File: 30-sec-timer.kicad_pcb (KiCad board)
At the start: 2 copper layers, 53.3 x 52.1 mm, 30 parts, among them P1 6.3V AC IN, P2 CL12345, P3 Right, P4 Left, Q1 BC557, Q2 BC547, U1 LM7805CT, U2 LM555N

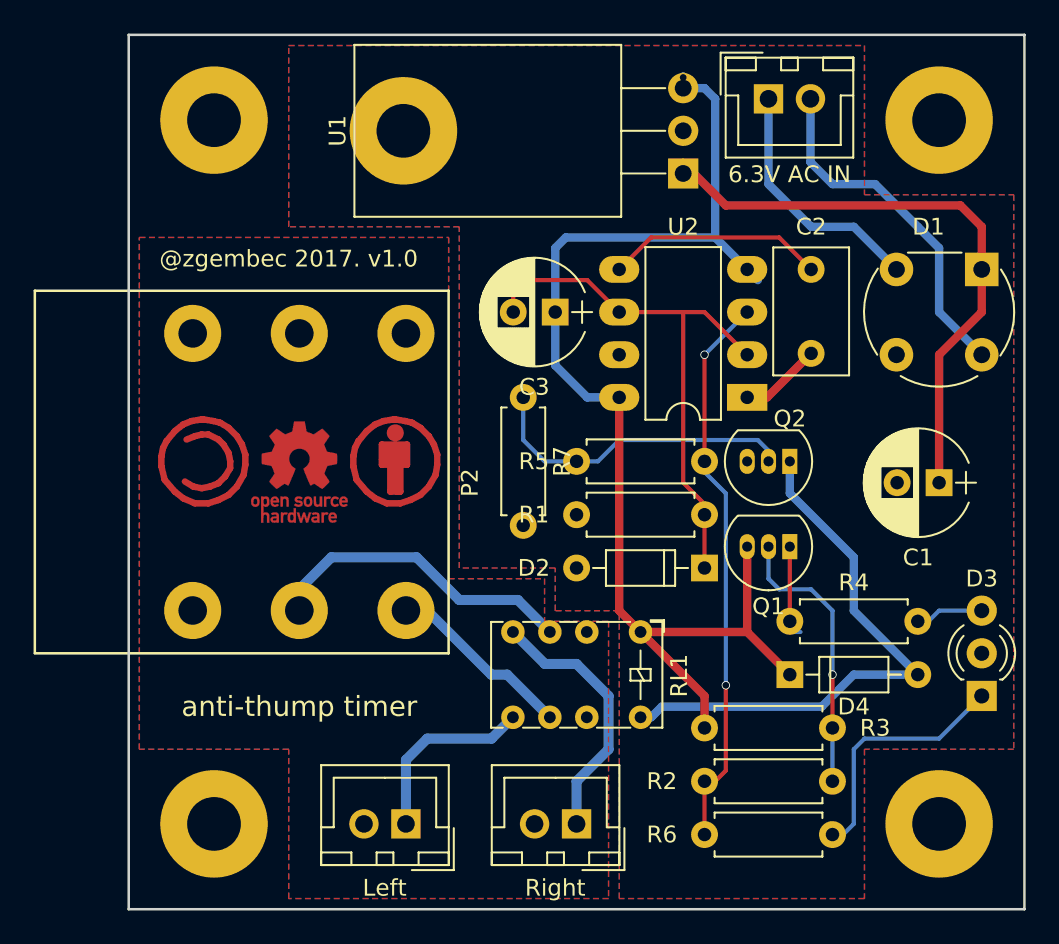
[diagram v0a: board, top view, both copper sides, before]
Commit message: resistor placement fix
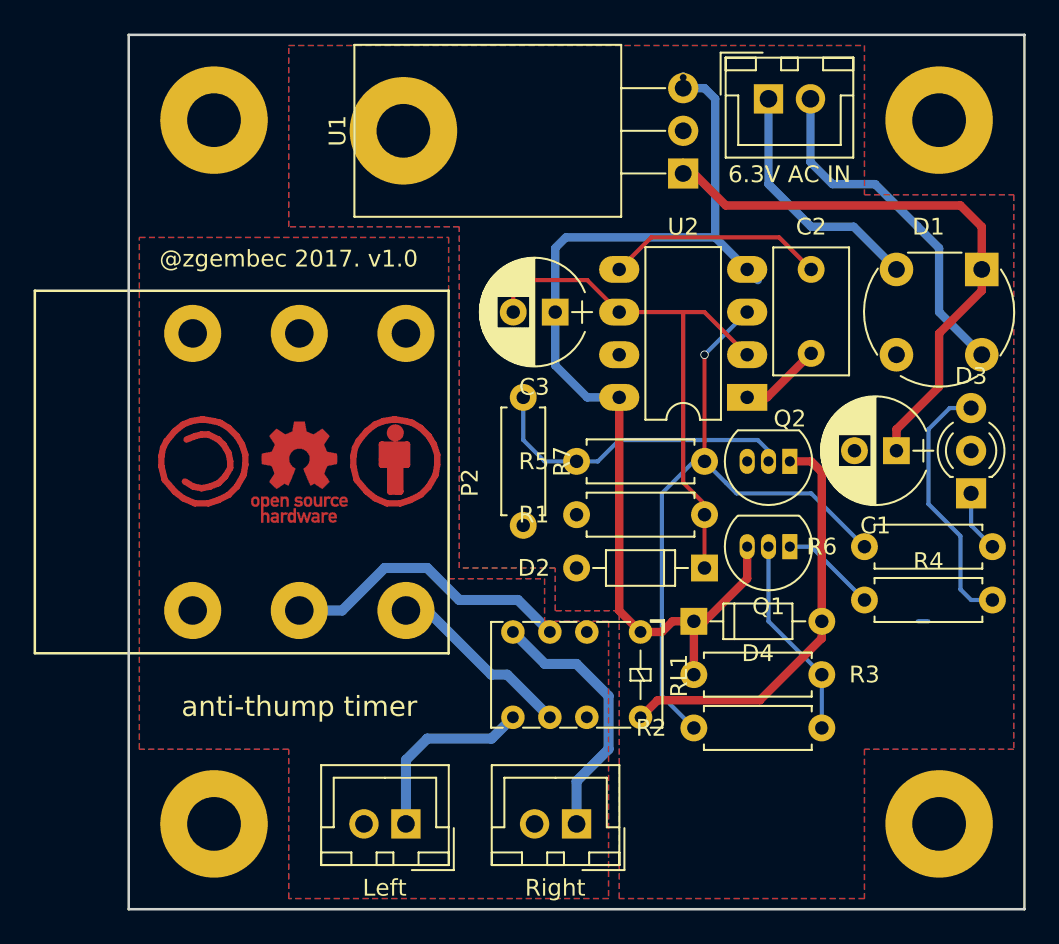
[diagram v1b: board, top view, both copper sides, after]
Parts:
- moved R6 19.6 mm to (186.1, 111.8)
- moved D3 12.1 mm to (192.4, 108.6)
- moved D4 6.54 mm to (175.9, 116.2)
- moved R4 4.62 mm to (186.1, 114.9)
- moved R3 3.24 mm to (175.9, 119.4)
- moved R2 3.24 mm to (183.5, 122.6)
- moved C1 3.17 mm to (188.0, 106.0)
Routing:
- net Net-(D3-Pad1): track 14.9 -> 3.70 mm
- net Net-(D3-Pad3): track 4.71 -> 15.5 mm
- net VCC: track 72.5 -> 62.9 mm
- net Net-(D4-Pad2): track 33.4 -> 24.8 mm
- net Net-(R2-Pad2): track 34.2 -> 40.9 mm, vias 3 -> 2
- net Net-(Q1-Pad2): track 16.7 -> 12.1 mm, vias 1 -> 0
- net Net-(C1-Pad1): track 35.7 -> 34.8 mm
- net Net-(Q1-Pad1): track 5.08 -> 5.76 mm
- net (no net): track 0.00 -> 0.64 mm
